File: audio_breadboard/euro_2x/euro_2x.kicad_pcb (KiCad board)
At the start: 2 copper layers, 182.9 x 121.9 mm, 39 parts, among them J1 EURO POWER, J10 IN, J11 IN, J12 OUT, J13 OUT, J14 AUX1, J15 AUX2, J16 IN, J17 OUT, J18 GND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

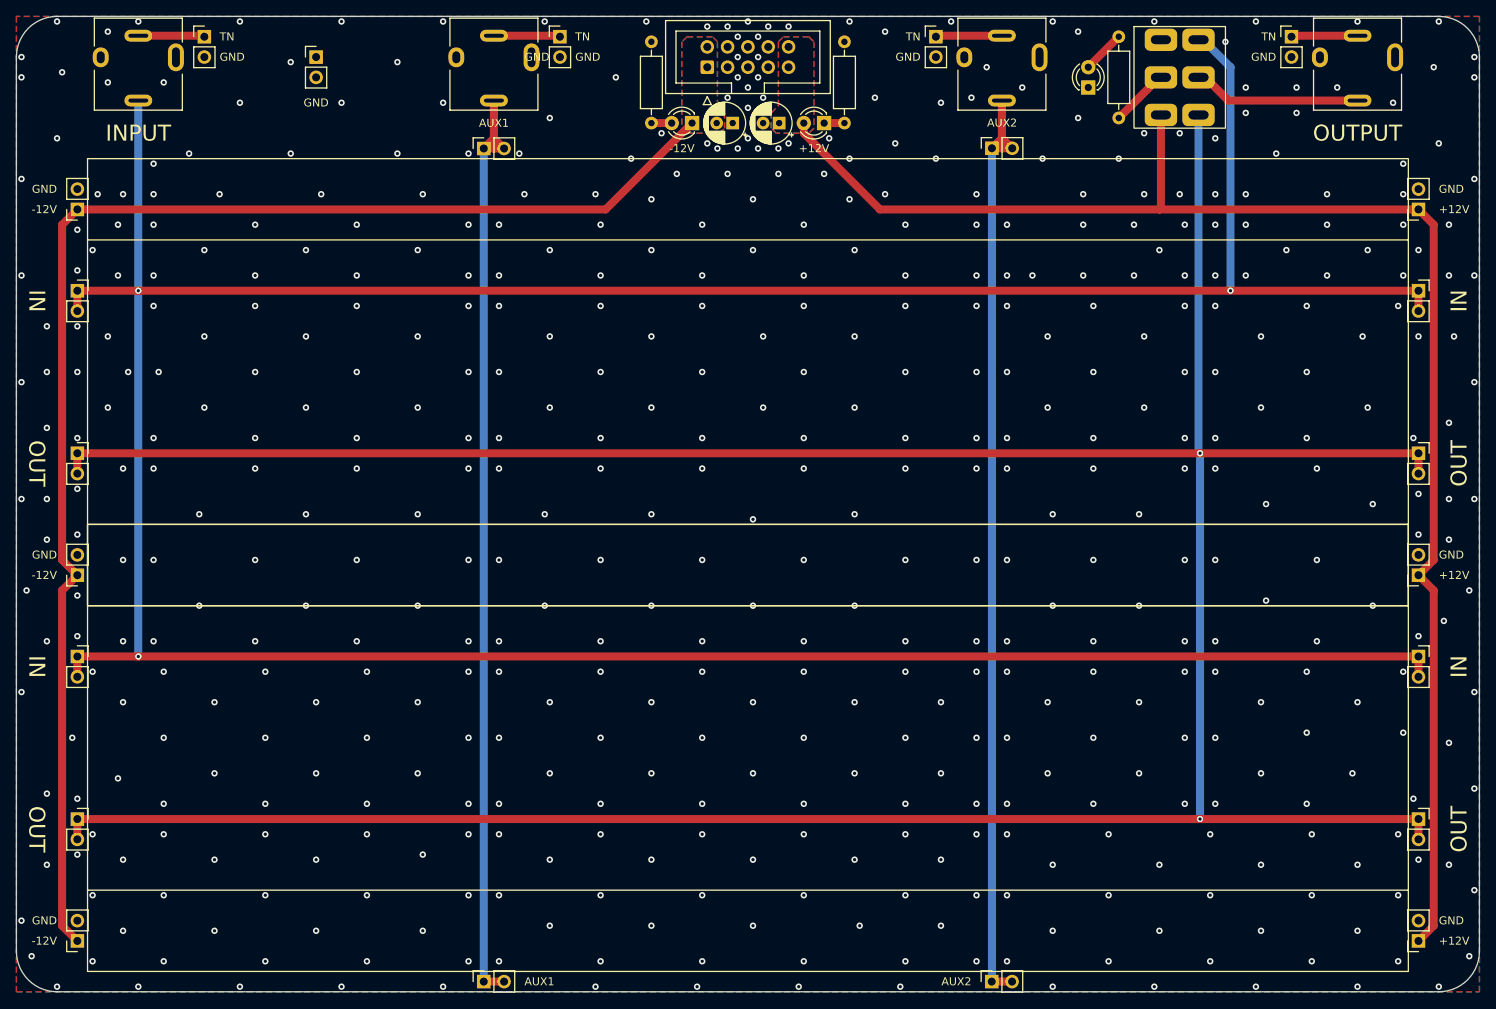
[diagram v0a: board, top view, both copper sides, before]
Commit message: fix breadboard footprint
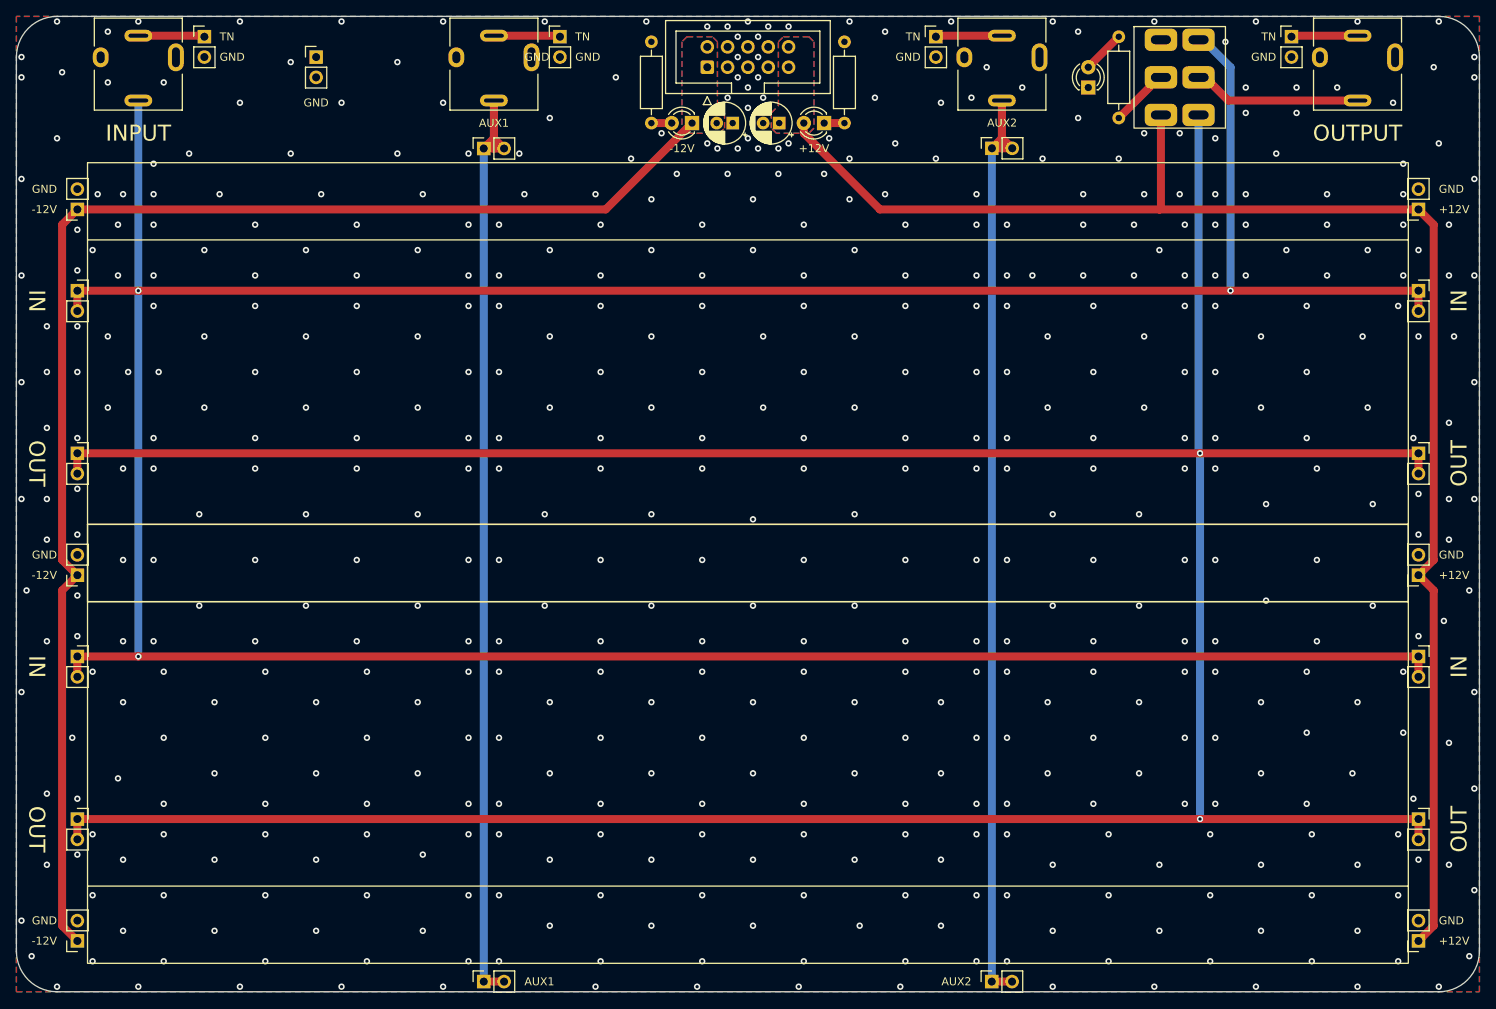
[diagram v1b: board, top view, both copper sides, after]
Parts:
- moved B2 0.51 mm to (152.4, 121.4)

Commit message: Finalize board layouts
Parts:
- moved J23 1.02 mm to (119.4, 150.1)
- moved J24 1.02 mm to (182.9, 150.1)
- moved J19 0.76 mm to (236.2, 145.3)
- moved J20 0.76 mm to (68.6, 145.3)
- moved J15 0.53 mm to (182.9, 47.5)
- moved J17 0.51 mm to (236.2, 130.3)
- moved J22 0.51 mm to (68.6, 130.3)
- moved J14 0.51 mm to (119.4, 47.5)
- moved J16 0.51 mm to (236.2, 110.0)
- moved J21 0.51 mm to (68.6, 110.0)
- moved J7 0.25 mm to (236.2, 100.1)
- moved J6 0.25 mm to (236.2, 54.9)
- moved J8 0.25 mm to (68.6, 54.9)
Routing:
- net /AUX2: track 123.5 -> 121.9 mm
- net +12V: track 188.5 -> 187.7 mm
- net -12V: track 175.9 -> 175.1 mm
- net /TO_OUT: track 433.5 -> 433.0 mm
- net /INPUT: track 448.3 -> 447.8 mm
- net /AUX1: track 123.5 -> 123.0 mm
- net GND: vias 519 -> 517
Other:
- board text added: "Audio Breadboard 2x Max Proskauer Jan 2024 v0.1 github.com/mprosk/audio_breadboard"
- board text added: "JLCJLCJLCJLC"
